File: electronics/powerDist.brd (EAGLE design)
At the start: 100 x 80 mm, 54 parts, among them CON1 B3B-ZR, IC1 TPS6300, IC2 TPS77033, J1 2MMPAD, J2 2MMPAD, J3 2MMPAD, J4 2MMPAD, J5 2MMPAD, J6 2MMPAD, J7 2MMPAD, J8 2MMPAD, J9 2MMPAD, U1 DRV8830, U2 MSP430F5500IRGZR, U3 DRV8830, U4 DRV8830

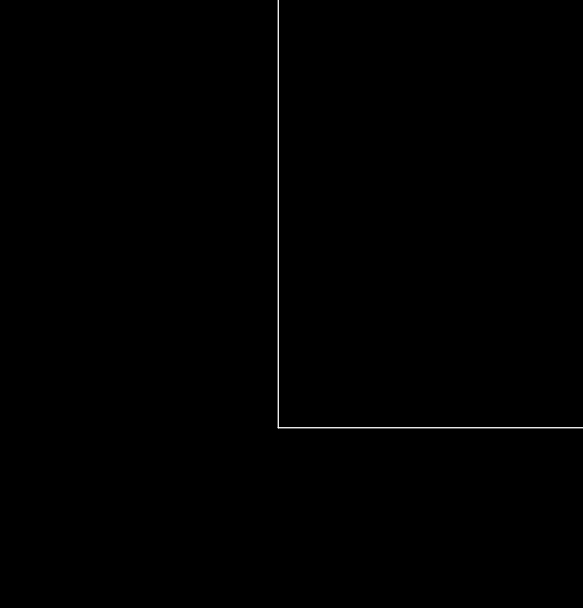
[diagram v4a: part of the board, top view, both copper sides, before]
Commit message: added single chip imu, need to hooking up.  Investigate i2c compatablity
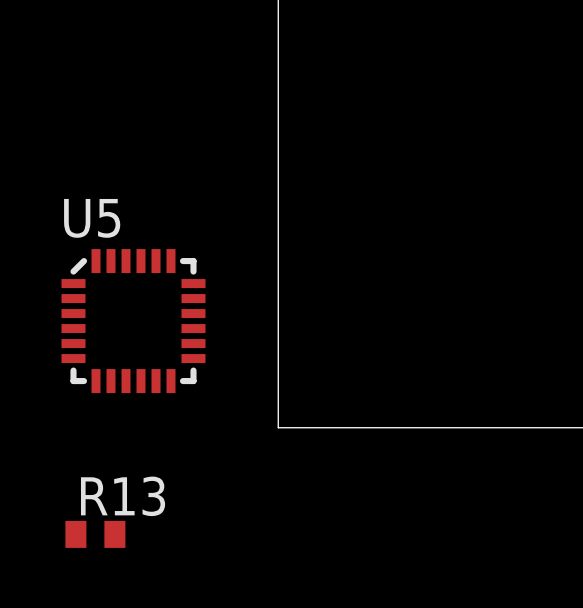
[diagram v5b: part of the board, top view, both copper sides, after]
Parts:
- added R13: 2k, rcl:R0402
- added U5: (no value), SparkFun-Sensors:QFN-24-NP
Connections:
- new net N$21: R13.2, U5.6, U5.7
- net +3V3: now also R13.1, U5.13, U5.3, U5.8
- net GND: now also U5.15, U5.17, U5.18, U5.9
- net MOTOR_SCL: now also U5.23
- net MOTOR_SDA: now also U5.24
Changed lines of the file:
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@@
 <element name="C22" library="rcl" package="C0603" value=".1uf" x="40.767" y="45.974"/>
 <element name="R12" library="rcl" package="R0402" value="100" x="40.64" y="44.45" rot="R180"/>
+<element name="U5" library="SparkFun-Sensors" package="QFN-24-NP" value="" x="-4.826" y="3.556"/>
+<element name="R13" library="rcl" package="R0402" value="2k" x="-6.096" y="-3.556"/>
 </elements>
 <signals>
@@
 <vertex x="52.07" y="53.34"/>
 </polygon>
+<contactref element="U5" pad="18"/>
+<contactref element="U5" pad="17"/>
+<contactref element="U5" pad="15"/>
+<contactref element="U5" pad="9"/>
 <wire x1="83.4" y1="66.04" x2="83.4" y2="76.2" width="0" layer="19" extent="1-1"/>
 <wire x1="81.9" y1="55.88" x2="83.4" y2="66.04" width="0" layer="19" extent="1-1"/>
@@
 <wire x1="38.1" y1="30.45" x2="39.05" y2="30.45" width="0" layer="19" extent="1-1"/>
 <wire x1="43.18" y1="33.02" x2="39.05" y2="30.45" width="0" layer="19" extent="1-1"/>
-<wire x1="41.617" y1="45.974" x2="42.91" y2="46.5595" width="0" layer="19" extent="1-16"/>
-<wire x1="37.6174" y1="42.8498" x2="38.1" y2="44.45" width="0" layer="19" extent="1-16"/>
-<wire x1="38.1" y1="42.3405" x2="37.6174" y2="42.8498" width="0" layer="19" extent="1-16"/>
-<wire x1="36.6268" y1="42.8498" x2="37.6174" y2="42.8498" width="0" layer="19" extent="1-1"/>
-<wire x1="39.624" y1="42.8498" x2="38.6" y2="42.3405" width="0" layer="19" extent="1-16"/>
-<wire x1="34.79" y1="42.3405" x2="36.6268" y2="42.8498" width="0" layer="19" extent="1-16"/>
-<wire x1="41.91" y1="42.3405" x2="41.91" y2="44.45" width="0" layer="19" extent="16-16"/>
-<wire x1="42.8498" y1="40.132" x2="41.91" y2="42.3405" width="0" layer="19" extent="1-16"/>
 <wire x1="44.87" y1="35.306" x2="43.18" y2="33.02" width="0" layer="19" extent="1-1"/>
 <wire x1="44.57" y1="37.52" x2="44.87" y2="35.306" width="0" layer="19" extent="1-1"/>
 <wire x1="42.8498" y1="36.6268" x2="44.57" y2="37.52" width="0" layer="19" extent="1-1"/>
+<wire x1="42.8498" y1="40.132" x2="44.57" y2="37.52" width="0" layer="19" extent="1-1"/>
+<wire x1="41.91" y1="42.3405" x2="42.8498" y2="40.132" width="0" layer="19" extent="1-16"/>
+<wire x1="41.91" y1="44.45" x2="41.91" y2="42.3405" width="0" layer="19" extent="16-16"/>
+<wire x1="41.617" y1="45.974" x2="41.91" y2="44.45" width="0" layer="19" extent="1-16"/>
+<wire x1="42.91" y1="46.5595" x2="41.617" y2="45.974" width="0" layer="19" extent="1-16"/>
+<wire x1="42.56" y1="48.006" x2="42.91" y2="46.5595" width="0" layer="19" extent="16-16"/>
+<wire x1="39.624" y1="42.8498" x2="41.91" y2="42.3405" width="0" layer="19" extent="1-16"/>
+<wire x1="38.6" y1="42.3405" x2="39.624" y2="42.8498" width="0" layer="19" extent="1-16"/>
+<wire x1="38.1" y1="42.3405" x2="38.6" y2="42.3405" width="0" layer="19" extent="16-16"/>
+<wire x1="37.6174" y1="42.8498" x2="38.1" y2="42.3405" width="0" layer="19" extent="1-16"/>
+<wire x1="36.6268" y1="42.8498" x2="37.6174" y2="42.8498" width="0" layer="19" extent="1-1"/>
+<wire x1="38.1" y1="44.45" x2="37.6174" y2="42.8498" width="0" layer="19" extent="1-16"/>
+<wire x1="34.79" y1="42.3405" x2="36.6268" y2="42.8498" width="0" layer="19" extent="1-16"/>
+<wire x1="34.29" y1="44.45" x2="34.79" y2="42.3405" width="0" layer="19" extent="16-16"/>
+<wire x1="39.1" y1="46.5595" x2="38.1" y2="44.45" width="0" layer="19" extent="16-16"/>
+<wire x1="38.75" y1="48.006" x2="39.1" y2="46.5595" width="0" layer="19" extent="16-16"/>
+<wire x1="35.29" y1="46.5595" x2="34.29" y2="44.45" width="0" layer="19" extent="16-16"/>
+<wire x1="34.94" y1="48.006" x2="35.29" y2="46.5595" width="0" layer="19" extent="16-16"/>
 <wire x1="39.37" y1="39.37" x2="38.6" y2="42.3405" width="0" layer="19" extent="1-16"/>
 <wire x1="37.6174" y1="35.8902" x2="39.37" y2="39.37" width="0" layer="19" extent="1-1"/>
 <wire x1="46.87" y1="41.22" x2="42.8498" y2="40.132" width="0" layer="19" extent="1-1"/>
 <wire x1="46.57" y1="43.434" x2="46.87" y2="41.22" width="0" layer="19" extent="1-1"/>
-<wire x1="31.25" y1="34.495" x2="27.94" y2="38.1" width="0" layer="19" extent="1-1"/>
-<wire x1="31.75" y1="31.545" x2="31.25" y2="34.495" width="0" layer="19" extent="1-1"/>
+<wire x1="31.75" y1="31.545" x2="38.1" y2="30.45" width="0" layer="19" extent="1-1"/>
+<wire x1="31.25" y1="34.495" x2="31.75" y2="31.545" width="0" layer="19" extent="1-1"/>
+<wire x1="27.94" y1="38.1" x2="31.25" y2="34.495" width="0" layer="19" extent="1-1"/>
+<wire x1="-2.826" y1="4.806" x2="34.29" y2="4.46" width="0" layer="19" extent="1-1"/>
+<wire x1="-2.826" y1="4.306" x2="-2.826" y2="4.806" width="0" layer="19" extent="1-1"/>
+<wire x1="-2.826" y1="3.306" x2="-2.826" y2="4.306" width="0" layer="19" extent="1-1"/>
+<wire x1="-5.076" y1="1.556" x2="-2.826" y2="3.306" width="0" layer="19" extent="1-1"/>
 </signal>
 <signal name="N$1">
@@
 <contactref element="U1" pad="10"/>
 <contactref element="U2" pad="31"/>
+<contactref element="U5" pad="23"/>
 <wire x1="39.99" y1="39.37" x2="40.91" y2="42.3405" width="0" layer="19" extent="16-16"/>
 <wire x1="39.624" y1="35.8902" x2="39.99" y2="39.37" width="0" layer="19" extent="1-16"/>
 <wire x1="37.1" y1="42.3405" x2="40.91" y2="42.3405" width="0" layer="19" extent="16-16"/>
 <wire x1="33.29" y1="42.3405" x2="37.1" y2="42.3405" width="0" layer="19" extent="16-16"/>
+<wire x1="-5.576" y1="5.556" x2="33.29" y2="42.3405" width="0" layer="19" extent="1-16"/>
 </signal>
 <signal name="MOTOR_SDA">
@@
 <contactref element="U1" pad="9"/>
 <contactref element="U2" pad="30"/>
+<contactref element="U5" pad="24"/>
 <wire x1="39.99" y1="40.64" x2="41.41" y2="42.3405" width="0" layer="19" extent="16-16"/>
 <wire x1="37.6" y1="42.3405" x2="39.99" y2="40.64" width="0" layer="19" extent="16-16"/>
 <wire x1="33.79" y1="42.3405" x2="37.6" y2="42.3405" width="0" layer="19" extent="16-16"/>
 <wire x1="39.116" y1="35.8902" x2="39.99" y2="40.64" width="0" layer="19" extent="1-16"/>
+<wire x1="-6.076" y1="5.556" x2="33.79" y2="42.3405" width="0" layer="19" extent="1-16"/>
 </signal>
 <signal name="SAT_SERIAL">
@@
 <vertex x="52.07" y="53.34"/>
 </polygon>
+<contactref element="U5" pad="8"/>
+<contactref element="U5" pad="13"/>
+<contactref element="U5" pad="3"/>
+<contactref element="R13" pad="1"/>
 <wire x1="81.7" y1="31.75" x2="81.7" y2="41.91" width="0" layer="19" extent="1-1"/>
 <wire x1="81.9" y1="26.67" x2="81.7" y2="31.75" width="0" layer="19" extent="1-1"/>
@@
 <wire x1="81.7" y1="1.27" x2="81.7" y2="6.35" width="0" layer="19" extent="1-1"/>
 <wire x1="44.68" y1="33.02" x2="81.7" y2="31.75" width="0" layer="19" extent="1-1"/>
-<wire x1="38.1254" y1="35.8902" x2="37.15" y2="33.05" width="0" layer="19" extent="1-1"/>
-<wire x1="37.1094" y1="42.8498" x2="41.29" y2="44.45" width="0" layer="19" extent="1-1"/>
+<wire x1="38.1254" y1="35.8902" x2="44.68" y2="33.02" width="0" layer="19" extent="1-1"/>
+<wire x1="37.15" y1="33.05" x2="38.1254" y2="35.8902" width="0" layer="19" extent="1-1"/>
+<wire x1="37.1094" y1="42.8498" x2="38.1254" y2="35.8902" width="0" layer="19" extent="1-1"/>
+<wire x1="41.29" y1="44.45" x2="37.1094" y2="42.8498" width="0" layer="19" extent="1-1"/>
+<wire x1="-2.826" y1="2.306" x2="37.15" y2="33.05" width="0" layer="19" extent="1-1"/>
+<wire x1="-5.576" y1="1.556" x2="-2.826" y2="2.306" width="0" layer="19" extent="1-1"/>
+<wire x1="-6.826" y1="3.806" x2="-5.576" y2="1.556" width="0" layer="19" extent="1-1"/>
+<wire x1="-6.746" y1="-3.556" x2="-5.576" y2="1.556" width="0" layer="19" extent="1-1"/>
 </signal>
 <signal name="N$3">
@@
 <wire x1="40.132" y1="42.8498" x2="39.99" y2="44.45" width="0" layer="19" extent="1-1"/>
 </signal>
+<signal name="N$21">
+<contactref element="U5" pad="7"/>
+<contactref element="U5" pad="6"/>
+<contactref element="R13" pad="2"/>
+<wire x1="-6.076" y1="1.556" x2="-5.446" y2="-3.556" width="0" layer="19" extent="1-1"/>
+<wire x1="-6.826" y1="2.306" x2="-6.076" y2="1.556" width="0" layer="19" extent="1-1"/>
+</signal>
 </signals>

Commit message: worked on imu layout/sch.
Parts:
- added C23, C24, C25: .1uf, rcl:C0603
- C1, C2: value (none) -> 10F
- moved R13 14.4 mm to (5.08, 5.59), turned to 90 degrees
- moved U5 13.7 mm to (7.62, 9.40)
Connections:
- net MOTOR_SCL renamed SYS_SCL
- net MOTOR_SDA renamed SYS_SDA
- new net IMU_INT: U2.17, U5.12
- new net N$22: C24.1, U5.10
- new net N$23: C25.1, U5.20
- net +3V3: now also C23.1
- net DRIVER_FAULT_1: now also U2.14
- net DRIVER_FAULT_2: now also U2.15
- net DRIVER_FAULT_3: now also U2.16
- net GND: now also C23.2, C24.2, C25.2, U5.1, U5.11
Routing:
- net GND: track 0.00 -> 11.8 mm, vias 0 -> 5
- net +3V3: track 0.00 -> 9.91 mm
- net N$21: track 0.00 -> 2.88 mm
- net N$22: track 0.00 -> 1.99 mm
- net N$23: track 0.00 -> 1.59 mm
- removed copper zone on layer 1, net +3V3

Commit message: continuing work on layout
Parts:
- added J10: 2MMPAD, connectors:2MMPAD
- C8: value 10uf -> .1uf
- moved C4 71.1 mm to (27.9, 30.7), turned to 90 degrees
- moved R7 66.7 mm to (29.5, 30.7), turned to 90 degrees
- moved J9 65.5 mm to (20.3, 49.8)
- moved C7 63.3 mm to (27.6, 34.7), turned to 180 degrees
- moved C16 61.9 mm to (33.8, 44.5), turned to 180 degrees
- moved C8 61.9 mm to (24.4, 31.0), flipped to the bottom, turned to 180 degrees
- moved C9 59.8 mm to (24.4, 33.0), flipped to the bottom, turned to 180 degrees
- moved C23 57.5 mm to (43.7, 49.0), flipped to the bottom, turned to 90 degrees
- moved C15 56.8 mm to (38.1, 46.7), turned to 180 degrees
- moved C24 56.7 mm to (46.2, 48.5), flipped to the bottom, turned to 180 degrees
- moved R13 56.7 mm to (42.2, 48.5), flipped to the bottom, turned to 270 degrees
- moved R8 55.8 mm to (34.8, 32.0), turned to 90 degrees
- moved C14 55.7 mm to (33.3, 42.4), turned to 180 degrees
- moved R9 54.8 mm to (34.8, 29.0), turned to 90 degrees
- moved C17 54.7 mm to (37.6, 32.5), turned to 180 degrees
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- renumbered U$1 to Q1
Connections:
- net GND: now also J10.P$1
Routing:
- net +5V: track 0.00 -> 27.7 mm
- net GND: track 11.8 -> 36.4 mm, vias 5 -> 3
- net SYS_SDA: track 0.00 -> 22.3 mm, vias 0 -> 1
- net SYS_SCL: track 0.00 -> 21.0 mm, vias 0 -> 1
- net N$15: track 0.00 -> 8.94 mm
- net N$2: track 0.00 -> 5.90 mm
- net +3V3: track 9.91 -> 15.5 mm
- net N$18: track 0.00 -> 5.03 mm
- net N$19: track 0.00 -> 4.96 mm
- net N$17: track 0.00 -> 4.85 mm
- net N$16: track 0.00 -> 4.10 mm
- net N$9: track 0.00 -> 3.64 mm
- net N$4: track 0.00 -> 3.55 mm
- net N$3: track 0.00 -> 3.55 mm
- net SAT_SERIAL: track 0.00 -> 3.21 mm
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- added copper zone on layer 1, net N$3
- added copper zone on layer 1, net N$4
- added copper zone on layer 1, net N$8
